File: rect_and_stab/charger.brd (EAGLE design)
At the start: 44 x 44 mm, 92 parts, among them Q1 BSZ0902NSI, Q2 BSZ0902NSI, Q3 FDN360P, Q4 BSZ0902NSI, Q5 BSZ0902NSI, Q6 BSS138, Q7 MOSFET-NCHANNEL2N7002PW, Q8 BSZ0902NSI, Q9 BSS138

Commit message: board routed and secondary protection removed
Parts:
- removed C23, C24, C25, C26, C27, C28: 0.1uF, resistor:C0402
- removed Q6: BSS138, SparkFun-DiscreteSemi:SOT323
- removed R30: 5.1k, resistor:R0402
- removed R32, R33, R34: 1k, resistor:R0402
- removed R35: 100, resistor:R0402
- removed R36: 20k, resistor:R0402
- removed U$17: SCP, SCP:SFD7A
- removed U$9: BQ2947, bq2947:BQ2947
- C9: value 1.5uF -> 2.2uF
- R25: device resistor:R2512 -> resistor:R2010
- moved R31 28.2 mm to (24.2, 13.6), turned to 90 degrees
- moved R15 24.9 mm to (27.5, 13.6), turned to 270 degrees
- moved U$1 24.0 mm to (23.1, 31.8)
- moved R17 22.7 mm to (26.4, 13.6), turned to 90 degrees
- moved D2 21.9 mm to (26.2, 26.9), turned to 0 degrees
- moved C8 20.7 mm to (29.1, 30.5), turned to 180 degrees
- moved JP2 20.1 mm to (15.0, 32.3), turned to 135 degrees
- moved C9 17.9 mm to (29.9, 26.6)
- moved C13 15.8 mm to (33.8, 8.63), turned to 225 degrees
- moved R24 14.6 mm to (33.0, 9.41), turned to 225 degrees
- moved R4 13.6 mm to (15.5, 35.6)
- moved R16 12.6 mm to (25.3, 13.6), turned to 90 degrees
- moved R27 12.5 mm to (23.1, 13.6), turned to 270 degrees
- moved R21 12.4 mm to (34.9, 10.5), turned to 315 degrees
- moved R5 12.0 mm to (21.2, 39.0)
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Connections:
- removed net N$46: C23.1, U$9.7
- removed net N$47: R30.1, R31.1, R36.2
- removed net N$48: R30.2, U$9.8
- removed net N$49: C25.2, C26.1, R33.1, U$9.4
- removed net N$50: C26.2, C27.1, R34.1, U$9.5
- removed net N$51: C25.1, R32.1, U$9.2, U$9.3
- removed net N$52: Q6.3, U$17.4
- removed net N$53: C24.1, R35.2, U$9.1
- removed net N$55: C28.2, Q6.1, R36.1
- net AGND: no longer C23.2, C24.2, C27.2, C28.1, Q6.2, U$9.6, U$9.9
- net GND: now also R31.1
- net N$26: no longer U$17.3
- net N$3: no longer R34.2
- net N$7: no longer R32.2, R35.1, U$17.1
- net N$8: no longer R33.2
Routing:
- net GND: track 0.00 -> 162.7 mm, vias 0 -> 49
- net AGND: track 0.00 -> 130.7 mm, vias 0 -> 2
- net N$45: track 0.00 -> 77.2 mm, vias 0 -> 2
- net N$59: track 0.00 -> 51.5 mm, vias 0 -> 2
- net N$41: track 0.00 -> 38.5 mm
- net N$28: track 0.00 -> 37.4 mm, vias 0 -> 2
- net N$34: track 0.00 -> 36.8 mm, vias 0 -> 2
- net N$10: track 0.00 -> 33.6 mm
- net N$39: track 0.00 -> 33.4 mm, vias 0 -> 2
- net N$7: track 0.00 -> 31.4 mm, vias 0 -> 1
- net N$4: track 0.00 -> 31.0 mm
- net N$26: track 0.00 -> 30.3 mm, vias 0 -> 2
- net N$35: track 0.00 -> 28.9 mm, vias 0 -> 2
- net N$21: track 0.00 -> 28.0 mm
- net N$29: track 0.00 -> 27.1 mm, vias 0 -> 2
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- added copper zone on layer 1, net GND
- added copper zone on layer 16, net GND

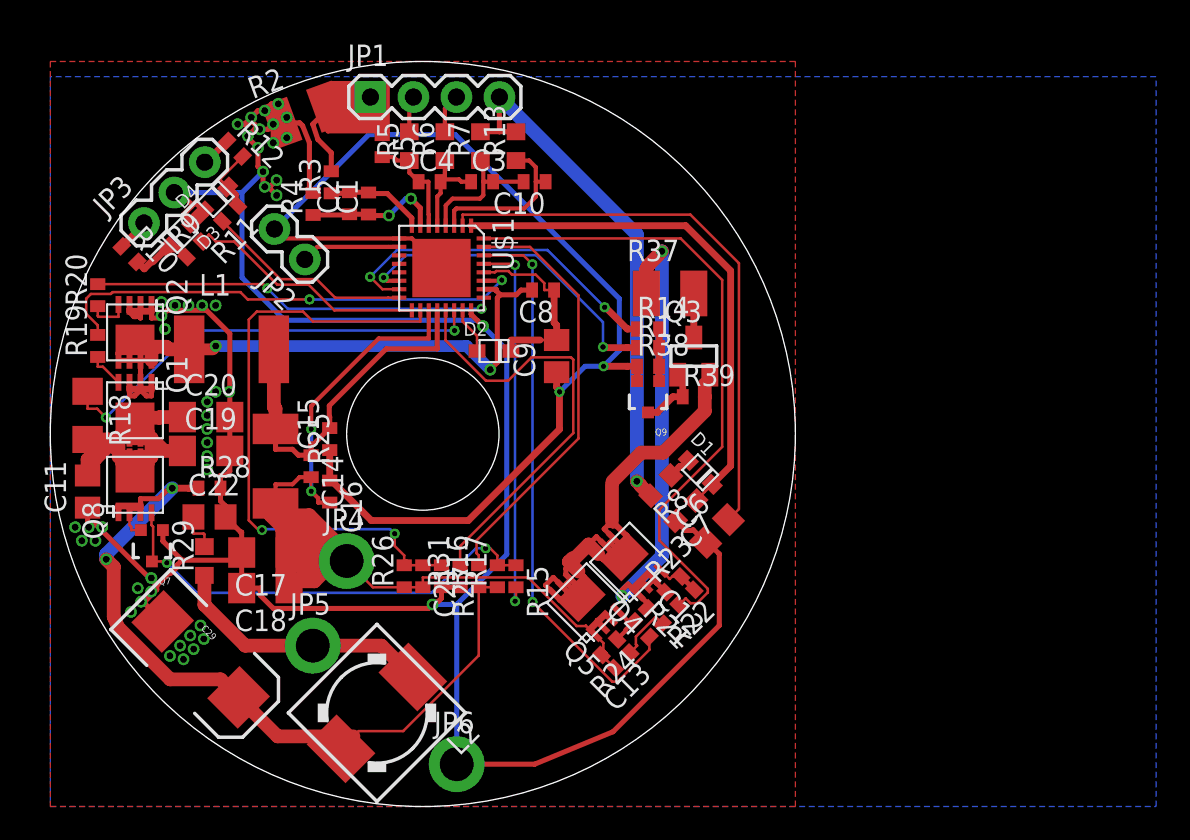
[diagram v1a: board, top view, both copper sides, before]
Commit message: mirrored charger board. this version has been ordered (charger&rect_and_stab)
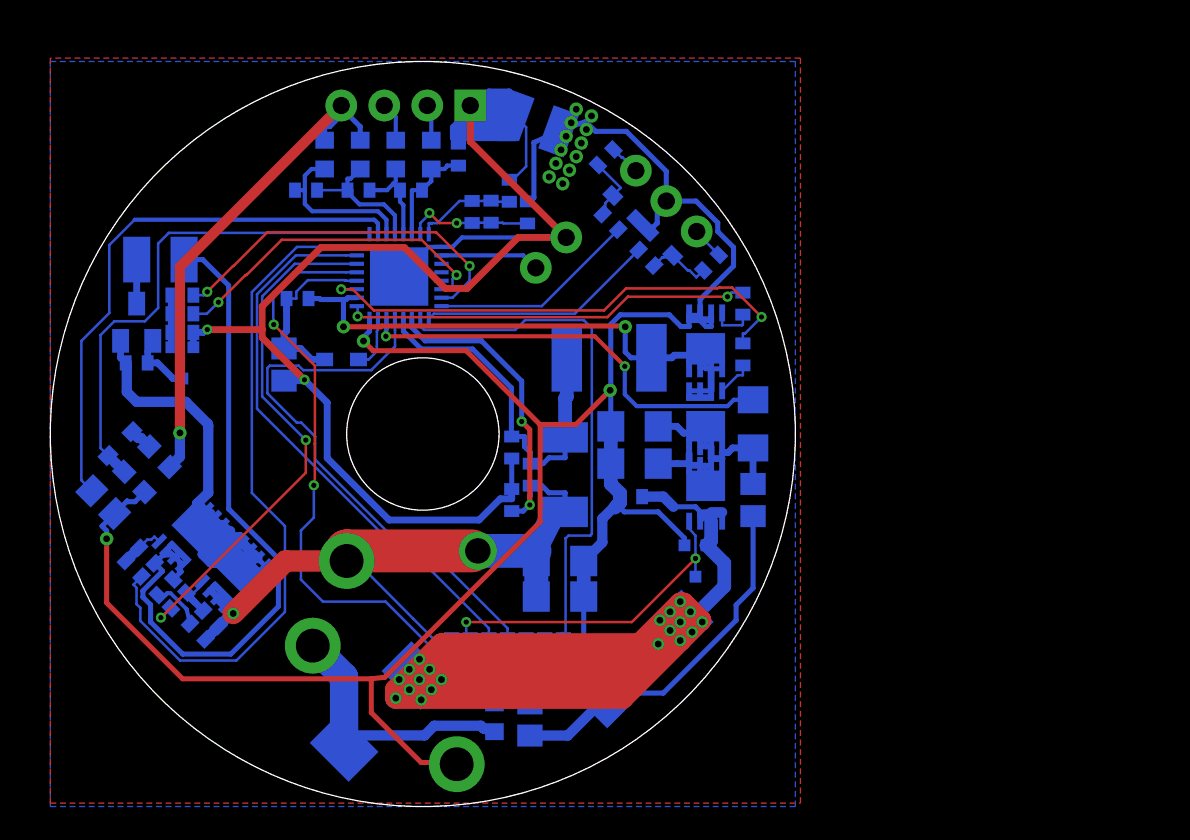
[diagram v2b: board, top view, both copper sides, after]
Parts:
- moved C11 39.3 mm to (41.5, 18.1), flipped to the bottom
- moved R18 39.3 mm to (41.5, 22.6), flipped to the bottom
- moved R19 38.1 mm to (40.9, 26.7), flipped to the bottom
- moved R20 38.1 mm to (40.9, 29.7), flipped to the bottom
- moved C6 36.3 mm to (3.13, 18.0), flipped to the bottom
- moved R10 34.3 mm to (39.0, 32.1), flipped to the bottom
- moved D1 34.3 mm to (4.12, 21.4), flipped to the bottom
- moved Q1 33.7 mm to (38.7, 22.9), flipped to the bottom
- moved Q2 33.7 mm to (38.7, 27.5), flipped to the bottom
- moved Q8 33.7 mm to (38.7, 18.5), flipped to the bottom
- moved Q3 33.0 mm to (5.10, 28.6), flipped to the bottom
- moved R39 33.0 mm to (5.10, 26.2), flipped to the bottom
- moved R22 32.7 mm to (4.93, 14.0), flipped to the bottom
- moved JP3 32.6 mm to (38.2, 34.0), flipped to the bottom
- moved C7 32.6 mm to (4.96, 19.2), flipped to the bottom
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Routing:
- net N$59: track 51.5 -> 142.8 mm, vias 2 -> 20
- net AGND: track 130.7 -> 113.8 mm
- net N$30: track 22.6 -> 35.3 mm
- net N$26: track 30.3 -> 42.1 mm, vias 2 -> 0
- net N$32: track 25.3 -> 33.2 mm
- net N$45: track 77.2 -> 69.6 mm, vias 2 -> 4
- net N$25: track 25.8 -> 32.7 mm
- net N$29: track 27.1 -> 20.6 mm
- net GND: track 162.7 -> 166.3 mm, vias 49 -> 15
- net N$28: track 37.4 -> 34.0 mm
- net N$21: track 28.0 -> 31.3 mm
- net N$34: track 36.8 -> 33.5 mm, vias 2 -> 0
- net N$39: track 33.4 -> 30.8 mm
- net N$41: track 38.5 -> 40.7 mm
- net N$4: track 31.0 -> 29.4 mm
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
